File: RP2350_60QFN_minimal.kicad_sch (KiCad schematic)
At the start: 43 parts, among them J1 USB_B_Micro, J2 Conn_02x18_Odd_Even, J3 Conn_02x18_Odd_Even, J4 SM03B-SRSS-TB, SW1 SW_Push, SW2 SW_Push, U1 RP2350_60QFN, U2 NCP1117-3.3_SOT223, U3 W25Q128JVS, Y1 ABM8-272-T3

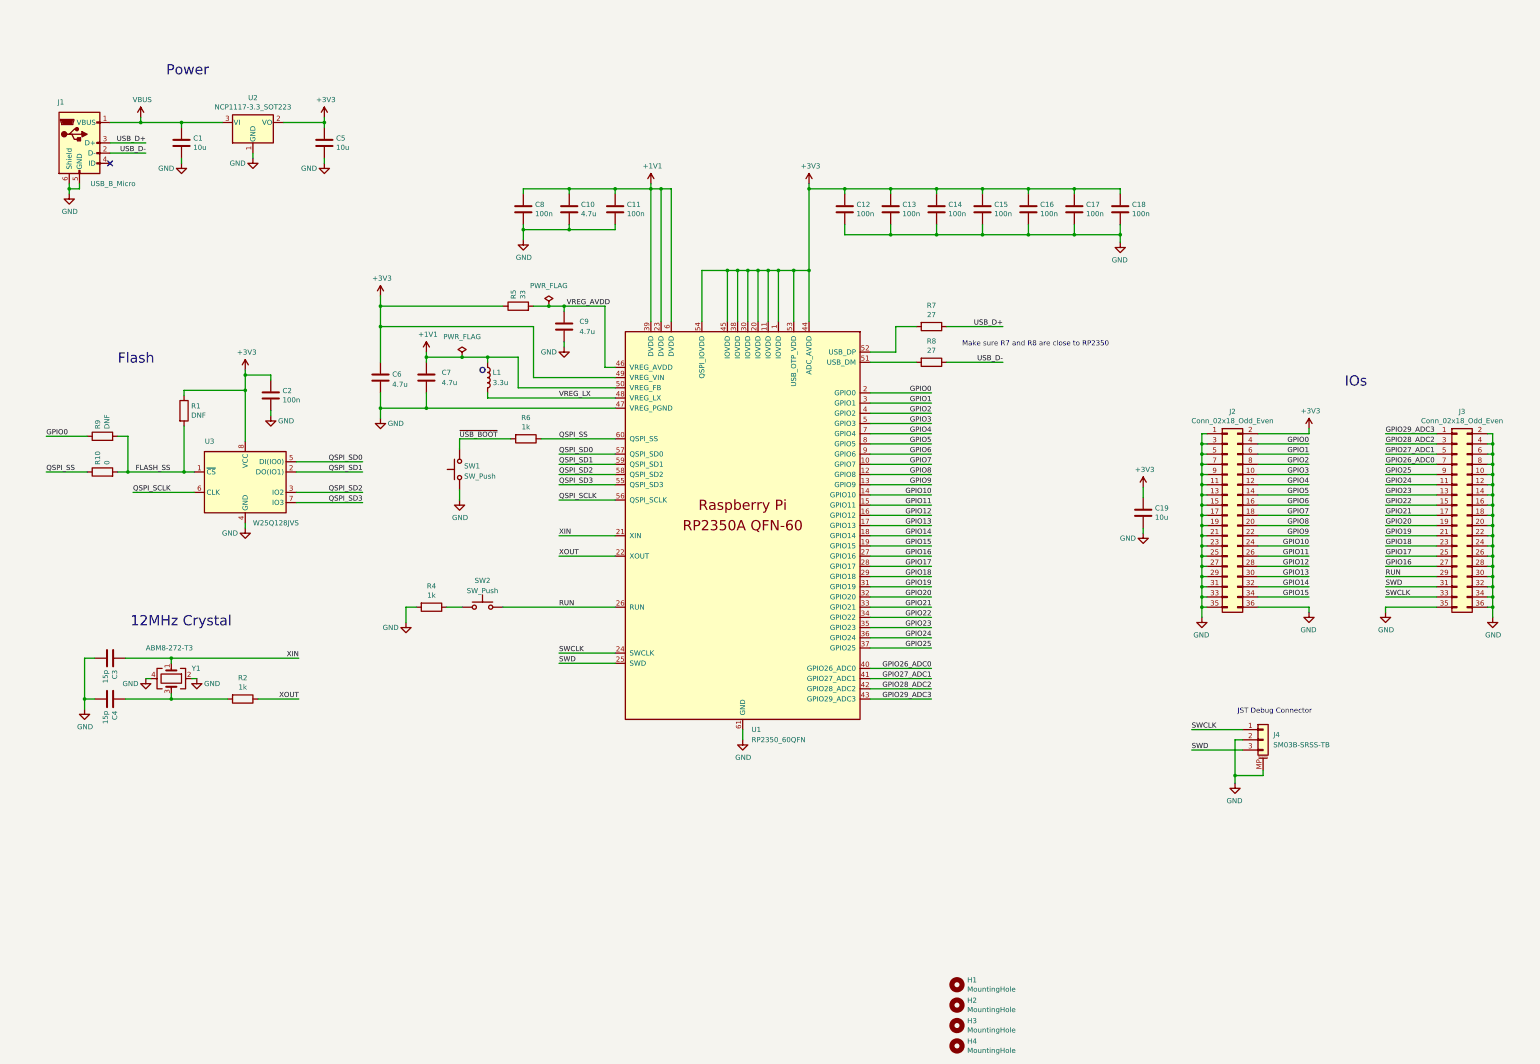
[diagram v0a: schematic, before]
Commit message: improve design
Improve design, added multiplexer
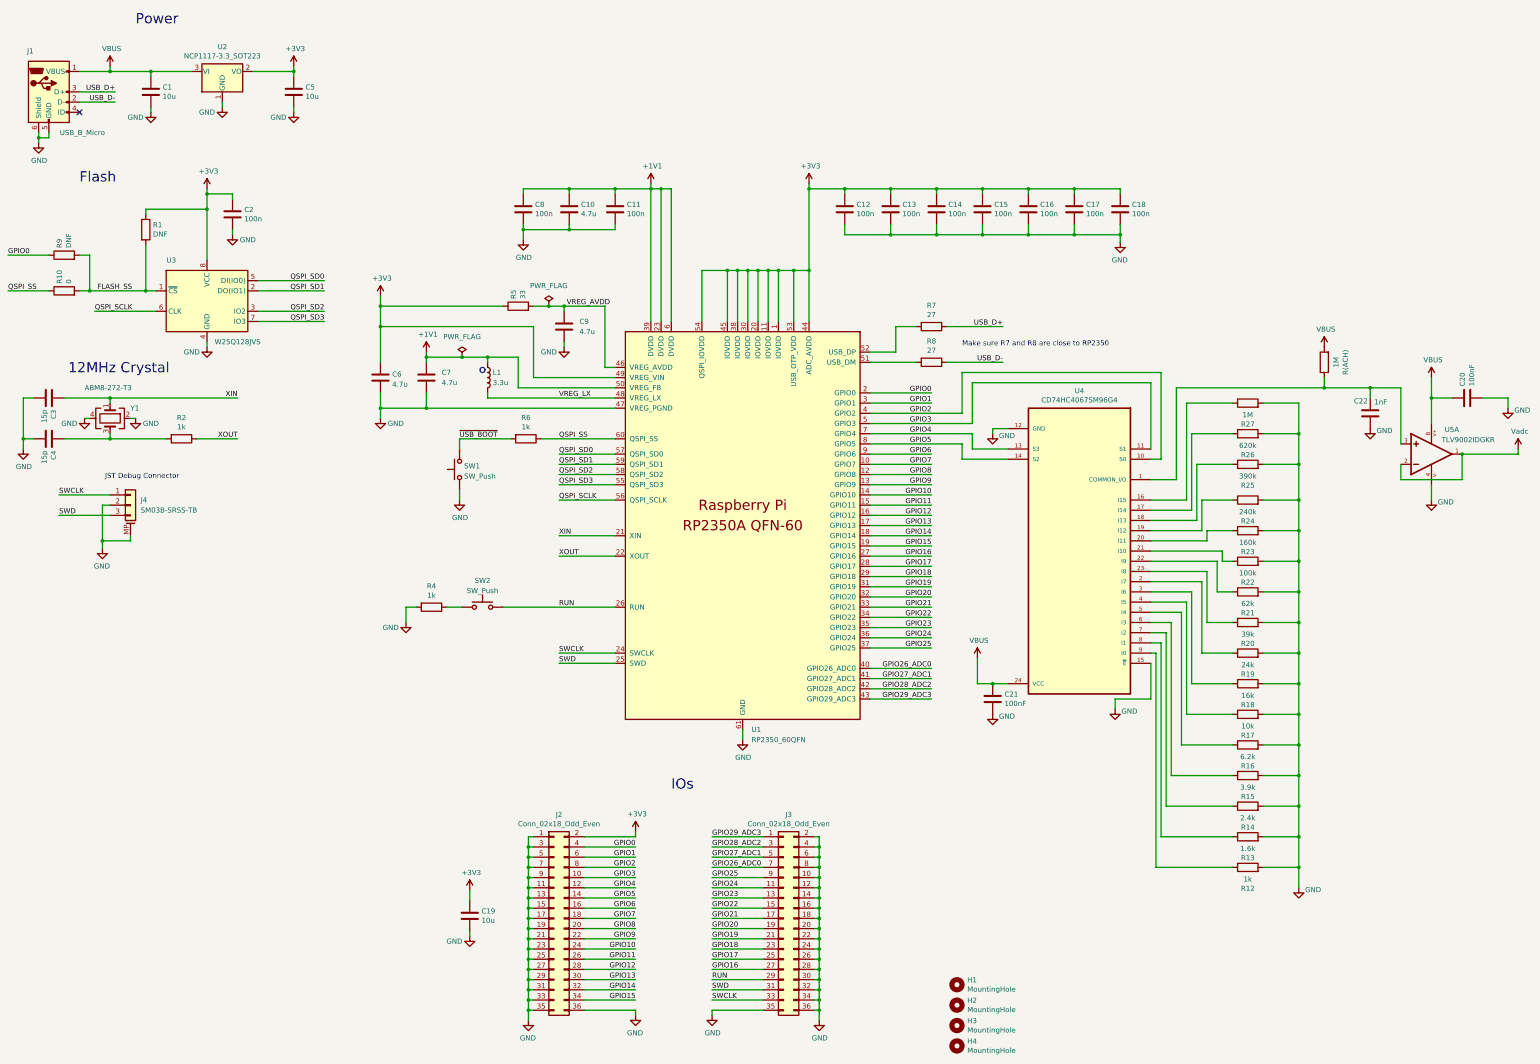
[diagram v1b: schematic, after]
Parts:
- added C20, C21: 100nF, Capacitor_SMD:C_0402_1005Metric, symbol Device:C
- added C22: 1nF, Capacitor_SMD:C_0402_1005Metric, symbol Device:C
- added R(ACH), R27: 1M, Resistor_SMD:R_0805_2012Metric_Pad1.20x1.40mm_HandSolder, symbol Device:R
- added R12: 1k, Resistor_SMD:R_0805_2012Metric_Pad1.20x1.40mm_HandSolder, symbol Device:R
- added R13: 1.6k, Resistor_SMD:R_0805_2012Metric_Pad1.20x1.40mm_HandSolder, symbol Device:R
- added R14: 2.4k, Resistor_SMD:R_0805_2012Metric_Pad1.20x1.40mm_HandSolder, symbol Device:R
- added R15: 3.9k, Resistor_SMD:R_0805_2012Metric_Pad1.20x1.40mm_HandSolder, symbol Device:R
- added R16: 6.2k, Resistor_SMD:R_0805_2012Metric_Pad1.20x1.40mm_HandSolder, symbol Device:R
- added R17: 10k, Resistor_SMD:R_0805_2012Metric_Pad1.20x1.40mm_HandSolder, symbol Device:R
- added R18: 16k, Resistor_SMD:R_0805_2012Metric_Pad1.20x1.40mm_HandSolder, symbol Device:R
- added R19: 24k, Resistor_SMD:R_0805_2012Metric_Pad1.20x1.40mm_HandSolder, symbol Device:R
- added R20: 39k, Resistor_SMD:R_0805_2012Metric_Pad1.20x1.40mm_HandSolder, symbol Device:R
- added R21: 62k, Resistor_SMD:R_0805_2012Metric_Pad1.20x1.40mm_HandSolder, symbol Device:R
- added R22: 100k, Resistor_SMD:R_0805_2012Metric_Pad1.20x1.40mm_HandSolder, symbol Device:R
- added R23: 160k, Resistor_SMD:R_0805_2012Metric_Pad1.20x1.40mm_HandSolder, symbol Device:R
- added R24: 240k, Resistor_SMD:R_0805_2012Metric_Pad1.20x1.40mm_HandSolder, symbol Device:R
- added R25: 390k, Resistor_SMD:R_0805_2012Metric_Pad1.20x1.40mm_HandSolder, symbol Device:R
- added R26: 620k, Resistor_SMD:R_0805_2012Metric_Pad1.20x1.40mm_HandSolder, symbol Device:R
- added U4: CD74HC4067SM96G4, CD74HC4067SM96G4:SOP65P780X200-24N, symbol CD74HC4067SM96G4:CD74HC4067SM96G4
- added U5: TLV9002IDGKR, TLV9002IDGKR:SOP65P490X110-8N, symbol TLV9002IDGKR:TLV9002IDGKR
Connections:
- net GND: now also C20.2, C21.2, C22.2, R12.2, R13.2, R14.2, R15.2, R16.2, R17.2, R18.2, R19.2, R20.2, R21.2, R22.2, R23.2, R24.2, R25.2, R26.2, R27.2, U4.12 (GND), U4.15 (~{E}), U5.4
- net GPIO2: now also U4.10 (S0)
- net GPIO3: now also U4.11 (S1)
- net GPIO4: now also U4.13 (S3)
- net GPIO5: now also U4.14 (S2)
- net VBUS: now also C20.1, C21.1, R(ACH).2, U4.24 (VCC), U5.8
- new net: R17.1, U4.4 (I5)
- new net: R21.1, U4.22 (I9)
- new net: R18.1, U4.3 (I6)
- new net: R15.1, U4.6 (I3)
- new net: C22.1, R(ACH).1, U4.1 (COMMON_I/O), U5.3
- new net: R27.1, U4.16 (I15)
- new net: R26.1, U4.17 (I14)
- new net: R25.1, U4.18 (I13)
- new net: R24.1, U4.19 (I12)
- new net: R19.1, U4.2 (I7)
- new net: R23.1, U4.20 (I11)
- new net: R22.1, U4.21 (I10)
- new net: R20.1, U4.23 (I8)
- new net: R16.1, U4.5 (I4)
- new net: R14.1, U4.7 (I2)
- new net: R13.1, U4.8 (I1)
- new net: R12.1, U4.9 (I0)
- new net Vadc: U5.1, U5.2
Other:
- moved on the sheet: C1, C19, C2, C3, C4, C5, J1, J2, J3, J4, R1, R10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

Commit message: Added adc signal processing, refactore hardware to blocks
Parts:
- removed C3, C4: 15p, Capacitor_SMD:C_0402_1005Metric, symbol Device:C
- removed R(ACH): 1M, Resistor_SMD:R_0805_2012Metric_Pad1.20x1.40mm_HandSolder, symbol Device:R
- removed R2: 1k, Resistor_SMD:R_0402_1005Metric, symbol Device:R
- removed R26: 620k, Resistor_SMD:R_0805_2012Metric_Pad1.20x1.40mm_HandSolder, symbol Device:R
- removed Y1: ABM8-272-T3, Crystal:Crystal_SMD_3225-4Pin_3.2x2.5mm, symbol Device:Crystal_GND24
- added C25: 1nF, Capacitor_SMD:C_0402_1005Metric, symbol Device:C
- added C26: 100nF, Capacitor_SMD:C_0402_1005Metric, symbol Device:C
- added GDT1: ~, 2031-42T-SM-RPLF:TVS_2031-42T-SM-RPLF, symbol 2031-42T-SM-RPLF:2031-42T-SM-RPLF
- added R(ACH)1, R3: 1M, Resistor_SMD:R_0805_2012Metric_Pad1.20x1.40mm_HandSolder, symbol Device:R
- added R11: 620k, Resistor_SMD:R_0805_2012Metric_Pad1.20x1.40mm_HandSolder, symbol Device:R
- added R26, R28: 10k, Resistor_SMD:R_0805_2012Metric_Pad1.20x1.40mm_HandSolder, symbol Device:R
- added R26: 1k, Resistor_SMD:R_0402_1005Metric, symbol Device:R
- added U6: ADS1115IDGSR, ADS1115IDGSR:SOP50P490X110-10N, symbol ADS1115IDGSR:ADS1115IDGSR
- added U7: PCA9306DP1_125, PCA9306DP1_125:SOP65P400X110-8N, symbol PCA9306DP1_125:PCA9306DP1_125
- added Y2: ABM8-272-T3, Crystal:Crystal_SMD_3225-4Pin_3.2x2.5mm, symbol Device:Crystal_GND24
- C20: value 100nF -> 15p
- C22: value 1nF -> 15p
- R12: value 1k -> 390k
- R13: value 1.6k -> 240k
- R14: value 2.4k -> 160k
- R15: value 3.9k -> 100k
- R16: value 6.2k -> 62k
- R17: value 10k -> 39k
- R18: value 16k -> 24k
- R19: value 24k -> 16k
- R20: value 39k -> 10k
- R21: value 62k -> 6.2k
- R22: value 100k -> 3.9k
- R23: value 160k -> 2.4k
- R24: value 240k -> 1.6k
- R25: value 390k -> 1k
- R27: value 1M -> 10k
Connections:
- net +3V3: now also GDT1.2, U7.2 (VREF1)
- net GND: now also C25.2, C26.2, R11.2, R26.1, R3.2, U6.3 (GND), Y2.2, Y2.4; no longer R27.2
- net GPIO2: no longer U1.4 (GPIO2), U4.10 (S0)
- net GPIO3: no longer U1.5 (GPIO3), U4.11 (S1)
- net GPIO4: no longer U1.7 (GPIO4), U4.13 (S3)
- net GPIO5: no longer U1.8 (GPIO5), U4.14 (S2)
- net GPIO6: no longer U1.9 (GPIO6)
- net GPIO7: no longer U1.10 (GPIO7)
- net VBUS: now also R27.2, C26.1, R(ACH)1.2, R28.2, U7.7 (VREF2); no longer C20.1
- net XIN: now also C20.1, Y2.1
- net XOUT: now also R26.1
- net at R17.1: now also U4.23 (I8); no longer U4.4 (I5)
- net at U4.22 (I9): now also R16.1; no longer R21.1
- net at R18.1: now also U4.2 (I7); no longer U4.3 (I6)
- net at R15.1: now also U4.21 (I10); no longer U4.6 (I3)
- net at U4.1 (COMMON_I/O), U5.3: now also C25.1, R(ACH)1.1; no longer C22.1
- net at R27.1: now also U6.8 (VDD); no longer U4.16 (I15)
- net at U4.17 (I14): now also R11.1
- net at R25.1: now also U4.9 (I0); no longer U4.18 (I13)
- net at U4.19 (I12): now also R13.1; no longer R24.1
- net at R19.1: now also U4.3 (I6); no longer U4.2 (I7)
- net at U4.20 (I11): now also R14.1; no longer R23.1
- net at R22.1: now also U4.6 (I3); no longer U4.21 (I10)
- net at R20.1: now also U4.4 (I5); no longer U4.23 (I8)
- net at U4.5 (I4): now also R21.1; no longer R16.1
- net at U4.7 (I2): now also R23.1; no longer R14.1
- net at U4.8 (I1): now also R24.1; no longer R13.1
- net at R12.1: now also U4.18 (I13); no longer U4.9 (I0)
- net Vadc renamed IN_ADC
- net IN_ADC: now also U6.4 (AIN0)
- new net: C22.1, R26.2, Y2.3
- new net: R3.1, U4.16 (I15)
- new net: R28.1, U6.2 (ALERT/RDY)
- new net: GDT1.1, R26.2, U6.1 (ADDR)
- new net I2C_SCL_3V3: U1.10 (GPIO7), U7.3 (SCL1)
- new net I2C_SCL_5V: U6.10 (SCL), U7.6 (SCL2)
- new net I2C_SDA_3V3: U1.9 (GPIO6), U7.4 (SDA1)
- new net I2C_SDA_5V: U6.9 (SDA), U7.5 (SDA2)
- new net MUX_SEL_0: U1.4 (GPIO2), U4.10 (S0)
- new net MUX_SEL_1: U1.5 (GPIO3), U4.11 (S1)
- new net MUX_SEL_2: U1.7 (GPIO4), U4.14 (S2)
- new net MUX_SEL_3: U1.8 (GPIO5), U4.13 (S3)
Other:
- note added: "ADC Processing"
- note added: "Attenuator / Range Selector"
- note added: "Mounting Holes"
- note removed: "Make sure R7 and R8 are close to RP2350"
- company: Raspberry Pi Ltd -> Smart Avtomatic
- title: RP2350A QFN-60 Minimal Design Example -> Gaz Logger
- moved on the sheet: C10, C11, C12, C13, C14, C15, C16, C17, C18, C19, C2, C8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

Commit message: added resistors matrics
added resistors matrics
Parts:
- GDT1: footprint 2031-42T-SM-RPLF:TVS_2031-42T-SM-RPLF -> Spark-2031-42T-SM-RPLF:TVS_2031-42T-SM-RPLF
- renumbered R26 to R27, R27 to R28, R28 to R29
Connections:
- net GPIO0: now also U4.10 (S0)
- net GPIO1: now also U4.11 (S1)
- net GPIO2: now also U1.4 (GPIO2), U4.14 (S2)
- net GPIO3: now also U1.5 (GPIO3), U4.13 (S3)
- net GPIO4: now also U1.7 (GPIO4), U7.4 (SDA1)
- net GPIO5: now also U1.8 (GPIO5), U7.3 (SCL1)
- net GPIO6: now also U1.9 (GPIO6)
- net GPIO7: now also U1.10 (GPIO7)
- removed net I2C_SCL_3V3: U1.10 (GPIO7), U7.3 (SCL1)
- removed net I2C_SDA_3V3: U1.9 (GPIO6), U7.4 (SDA1)
- removed net MUX_SEL_0: U1.4 (GPIO2), U4.10 (S0)
- removed net MUX_SEL_1: U1.5 (GPIO3), U4.11 (S1)
- removed net MUX_SEL_2: U1.7 (GPIO4), U4.14 (S2)
- removed net MUX_SEL_3: U1.8 (GPIO5), U4.13 (S3)
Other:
- note added: "MCU"
- moved on the sheet: C19, J2

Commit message: finish first design
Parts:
- added R30, R31: 4.7k, Resistor_SMD:R_0805_2012Metric_Pad1.20x1.40mm_HandSolder, symbol Device:R
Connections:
- net +3V3: now also R30.2, R31.2
- net GPIO4: now also R31.1
- net GPIO5: now also R30.1
